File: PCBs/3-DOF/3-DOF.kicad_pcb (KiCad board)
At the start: 2 copper layers, 57.2 x 50 mm, 11 parts, among them J1 Conn_02x07_Odd_Even, J2 Conn_02x08_Odd_Even, J3 Conn_02x08_Odd_Even, J4 Conn_01x02, J5 Conn_01x03_Pin, J6 Conn_01x02, J7 Conn_01x02, U1 MAX485E, U2 L298N

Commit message: updated with laser + servo + 485MAX (corrected
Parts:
- added C3: 10u, Capacitor_SMD:C_0402_1005Metric_Pad0.74x0.62mm_HandSolder, F.Cu at (193.7, 70.4)
- added C4: 10u, Capacitor_SMD:C_0402_1005Metric_Pad0.74x0.62mm_HandSolder, F.Cu at (193.7, 72.4)
- added C5: 10u, Capacitor_SMD:C_0402_1005Metric_Pad0.74x0.62mm_HandSolder, F.Cu at (193.7, 74.4)
- added J10: Conn_01x06, Connector_JST:JST_XH_S6B-XH-A_1x06_P2.50mm_Horizontal, F.Cu at (116.4, 81.0)
- added J11: Conn_01x04, Connector_JST:JST_XH_S4B-XH-A_1x04_P2.50mm_Horizontal, F.Cu at (175.1, 72.8)
- added J12: Conn_01x04, Connector_JST:JST_XH_S4B-XH-A_1x04_P2.50mm_Horizontal, F.Cu at (151.0, 39.4)
- added J13: Conn_01x03, Connector_JST:JST_XH_S3B-XH-A_1x03_P2.50mm_Horizontal, F.Cu at (192.8, 82.3)
- added J14: Conn_01x04, Connector_JST:JST_XH_S4B-XH-A_1x04_P2.50mm_Horizontal, F.Cu at (179.6, 39.4)
- added J15: Conn_01x04, Connector_JST:JST_XH_S4B-XH-A_1x04_P2.50mm_Horizontal, F.Cu at (165.3, 39.4)
- added J16: Conn_01x04, Connector_JST:JST_XH_S4B-XH-A_1x04_P2.50mm_Horizontal, F.Cu at (193.9, 39.4)
- added J17: Conn_01x04, Connector_JST:JST_XH_S4B-XH-A_1x04_P2.50mm_Horizontal, F.Cu at (99.7, 40.5)
- added J18: Conn_01x04, Connector_JST:JST_XH_S4B-XH-A_1x04_P2.50mm_Horizontal, F.Cu at (184.7, 89.2)
- added J8: Conn_01x06, Connector_JST:JST_XH_S6B-XH-A_1x06_P2.50mm_Horizontal, F.Cu at (136.6, 84.7)
- added J9: Conn_01x04, Connector_JST:JST_XH_S4B-XH-A_1x04_P2.50mm_Horizontal, F.Cu at (136.7, 39.4)
- added Q1: 2N7000, Package_TO_SOT_THT:TO-92_Inline, F.Cu at (191.6, 57.1)
- added R1: 1k, Resistor_SMD:R_0402_1005Metric_Pad0.72x0.64mm_HandSolder, F.Cu at (200.6, 59.5)
- added R2: 100, Resistor_SMD:R_0402_1005Metric_Pad0.72x0.64mm_HandSolder, F.Cu at (200.6, 61.5)
- added U3: L298N, Package_TO_SOT_THT:TO-220-15_P2.54x5.08mm_StaggerOdd_Lead4.58mm_Vertical, F.Cu at (166.7, 74.3)
- J5: value Conn_01x03_Pin -> Conn_01x02; footprint Connector_JST:JST_XH_S3B-XH-A_1x03_P2.50mm_Horizontal -> Connector_JST:JST_XH_S2B-XH-A_1x02_P2.50mm_Horizontal
- J6, J7: value Conn_01x02 -> Conn_01x06; footprint Connector_JST:JST_XH_S2B-XH-A_1x02_P2.50mm_Horizontal -> Connector_JST:JST_XH_S6B-XH-A_1x06_P2.50mm_Horizontal
- moved J4 67.2 mm to (103.5, 82.3), turned to 0 degrees
- moved J6 61.2 mm to (115.2, 41.8)
- moved J5 56.8 mm to (96.6, 72.7), turned to 90 degrees
- moved C2 46.1 mm to (193.7, 68.5), turned to 0 degrees
- moved C1 41.8 mm to (193.7, 66.5), turned to 0 degrees
- moved U2 37.6 mm to (119.1, 74.3), turned to 90 degrees
- moved U1 37.0 mm to (178.7, 56.5)
- moved J7 10.8 mm to (158.1, 79.9)
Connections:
- C2 pad 1: Net-(J5-Pin_1) -> GND
- C2 pad 2: unconnected-(C2-Pad2) -> +5V
- J5 pad 1: Net-(J5-Pin_1) -> +24V
- J6 pad 2: Net-(J6-Pin_2) -> GND
- J7 pad 2: Net-(J7-Pin_2) -> GND
- U1 pad 1: unconnected-(U1-RO-Pad1) -> /52
- U1 pad 2: unconnected-(U1-~{RE}-Pad2) -> /53
- U1 pad 3: unconnected-(U1-DE-Pad3) -> /53
- U1 pad 4: unconnected-(U1-DI-Pad4) -> /51
- U1 pad 6: unconnected-(U1-A-Pad6) -> Net-(J11-Pin_3)
- U1 pad 7: unconnected-(U1-B-Pad7) -> Net-(J11-Pin_2)
- U2 pad 10: /37 -> /10
- U2 pad 11: /42 -> /55
- U2 pad 12: /26 -> /11
- U2 pad 14: Net-(J7-Pin_2) -> Net-(J7-Pin_6)
- U2 pad 3: Net-(J6-Pin_2) -> Net-(J6-Pin_6)
- U2 pad 4: unconnected-(U2-Vs-Pad4) -> +24V
- U2 pad 5: /35 -> /8
- U2 pad 6: /41 -> /21
- U2 pad 7: /36 -> /9
- U2 pad 9: unconnected-(U2-Vss-Pad9) -> +5V
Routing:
- net +5V: track 23.3 -> 0.00 mm
- net Net-(J5-Pin_1): track 20.7 -> 0.00 mm
- net /27: track 16.1 -> 0.00 mm
- net GND: track 1.25 -> 0.00 mm, vias 1 -> 0
- removed copper zone on B.Cu, net GND
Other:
- board outline removed

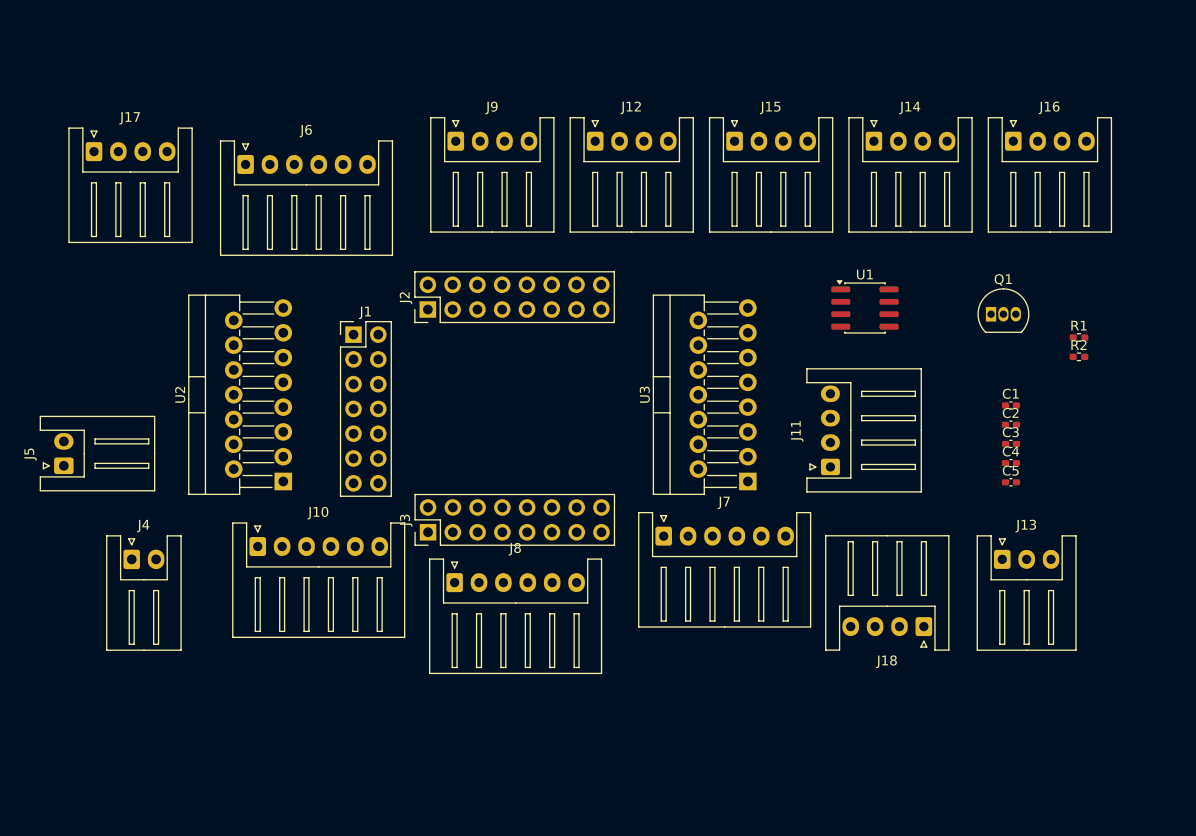
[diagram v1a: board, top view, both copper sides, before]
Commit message: fix RS485 + servo, add 10u cap's
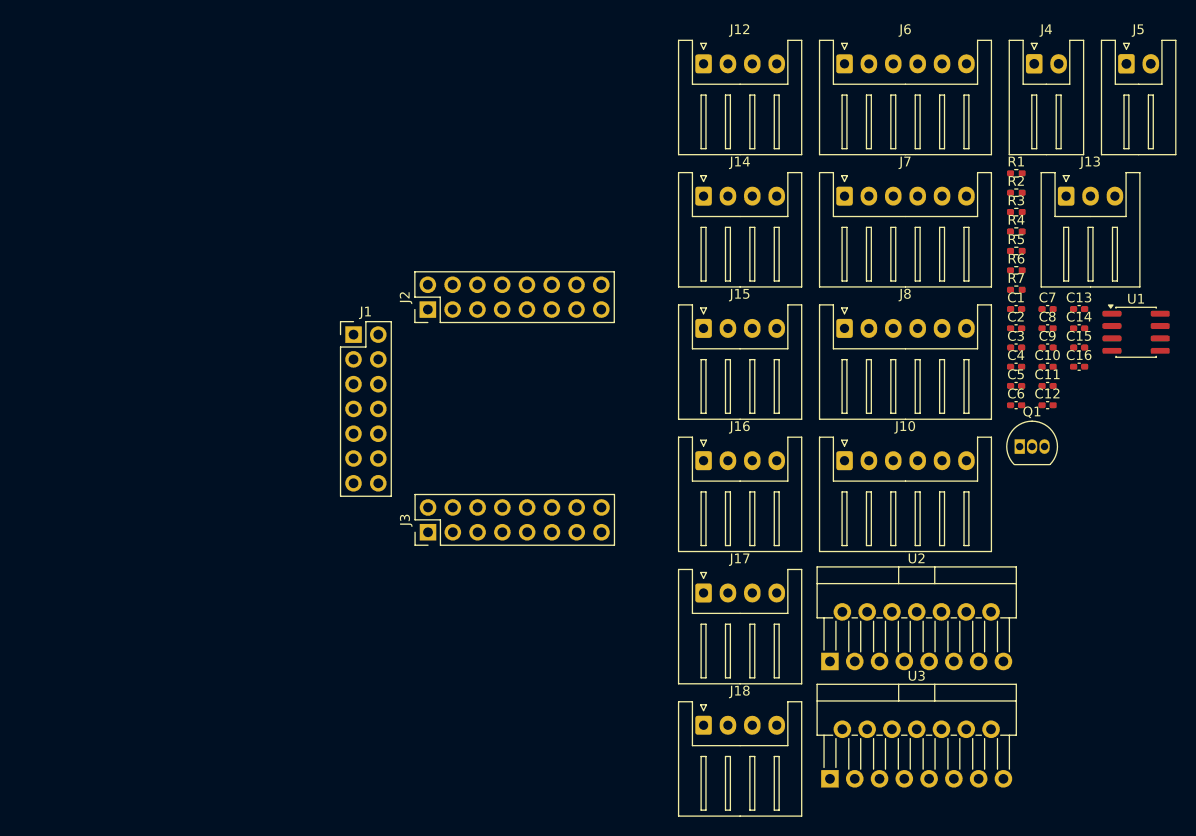
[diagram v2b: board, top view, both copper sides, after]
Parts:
- removed J11, J9: Conn_01x04, Connector_JST:JST_XH_S4B-XH-A_1x04_P2.50mm_Horizontal
- added C10: 10u, Capacitor_SMD:C_0402_1005Metric_Pad0.74x0.62mm_HandSolder, F.Cu at (197.4, 62.5)
- added C11: 10u, Capacitor_SMD:C_0402_1005Metric_Pad0.74x0.62mm_HandSolder, F.Cu at (197.4, 64.5)
- added C12: 10u, Capacitor_SMD:C_0402_1005Metric_Pad0.74x0.62mm_HandSolder, F.Cu at (197.4, 66.5)
- added C13: 10u, Capacitor_SMD:C_0402_1005Metric_Pad0.74x0.62mm_HandSolder, F.Cu at (200.6, 56.6)
- added C14: 10u, Capacitor_SMD:C_0402_1005Metric_Pad0.74x0.62mm_HandSolder, F.Cu at (200.6, 58.6)
- added C15: 10u, Capacitor_SMD:C_0402_1005Metric_Pad0.74x0.62mm_HandSolder, F.Cu at (200.6, 60.6)
- added C16: 10u, Capacitor_SMD:C_0402_1005Metric_Pad0.74x0.62mm_HandSolder, F.Cu at (200.6, 62.5)
- added C6: 100n, Capacitor_SMD:C_0402_1005Metric_Pad0.74x0.62mm_HandSolder, F.Cu at (194.2, 66.5)
- added C7: 10u, Capacitor_SMD:C_0402_1005Metric_Pad0.74x0.62mm_HandSolder, F.Cu at (197.4, 56.6)
- added C8: 10u, Capacitor_SMD:C_0402_1005Metric_Pad0.74x0.62mm_HandSolder, F.Cu at (197.4, 58.6)
- added C9: 10u, Capacitor_SMD:C_0402_1005Metric_Pad0.74x0.62mm_HandSolder, F.Cu at (197.4, 60.6)
- added R3: 10K, Resistor_SMD:R_0402_1005Metric_Pad0.72x0.64mm_HandSolder, F.Cu at (194.2, 46.7)
- added R4: 10K, Resistor_SMD:R_0402_1005Metric_Pad0.72x0.64mm_HandSolder, F.Cu at (194.2, 48.7)
- added R5: 20K, Resistor_SMD:R_0402_1005Metric_Pad0.72x0.64mm_HandSolder, F.Cu at (194.2, 50.7)
- added R6: 20K, Resistor_SMD:R_0402_1005Metric_Pad0.72x0.64mm_HandSolder, F.Cu at (194.2, 52.7)
- added R7: 120, Resistor_SMD:R_0402_1005Metric_Pad0.72x0.64mm_HandSolder, F.Cu at (194.2, 54.6)
- R1: value 1k -> 10K
- moved J5 116.5 mm to (205.5, 31.5), turned to 0 degrees
- moved J4 105.5 mm to (196.0, 31.5)
- moved J17 77.1 mm to (162.1, 85.7)
- moved J6 62.3 mm to (176.6, 31.5)
- moved J10 60.8 mm to (176.6, 72.2)
- moved U2 59.0 mm to (175.1, 92.7), turned to 0 degrees
- moved J8 47.7 mm to (176.6, 58.6)
- moved J16 45.6 mm to (162.1, 72.2)
- moved J7 39.5 mm to (176.6, 45.0)
- moved J13 37.8 mm to (199.3, 45.0)
- moved U3 31.6 mm to (175.1, 104.8), turned to 0 degrees
- moved U1 27.9 mm to (206.5, 59.0)
- moved J18 24.7 mm to (162.1, 99.3), turned to 0 degrees
- moved J15 19.4 mm to (162.1, 58.6)
- moved J14 18.3 mm to (162.1, 45.0)
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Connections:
- J12 pad 2: Net-(J11-Pin_2) -> Net-(J12-Pin_2)
- J12 pad 3: Net-(J11-Pin_3) -> Net-(J12-Pin_3)
- J14 pad 4: unconnected-(J14-Pin_4-Pad4) -> /26
- J15 pad 4: unconnected-(J15-Pin_4-Pad4) -> /27
- J16 pad 4: unconnected-(J16-Pin_4-Pad4) -> /28
- R1 pad 1: Net-(J11-Pin_3) -> +5V
- R1 pad 2: Net-(J11-Pin_2) -> /51
- U1 pad 6: Net-(J11-Pin_3) -> Net-(J12-Pin_2)
- U1 pad 7: Net-(J11-Pin_2) -> Net-(J12-Pin_3)
